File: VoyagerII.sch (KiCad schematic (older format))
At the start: 13 parts, among them U1 ATXMEGA32A4U-AU

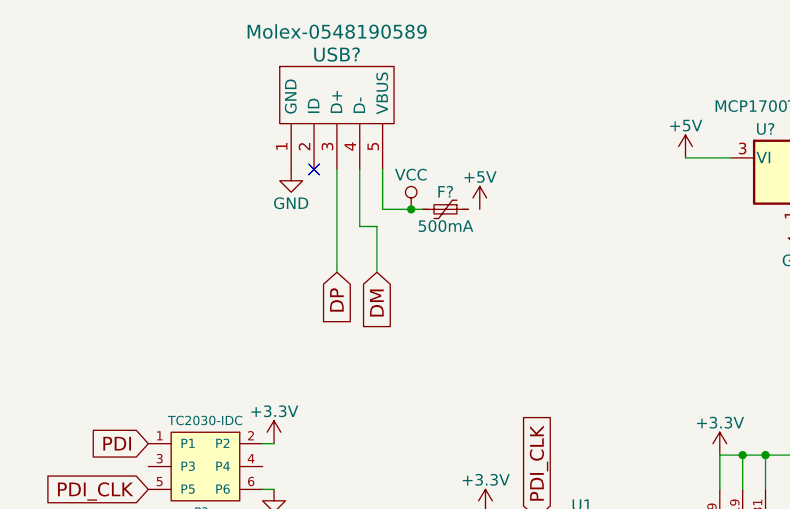
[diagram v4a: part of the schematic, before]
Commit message: Implement ESD protection
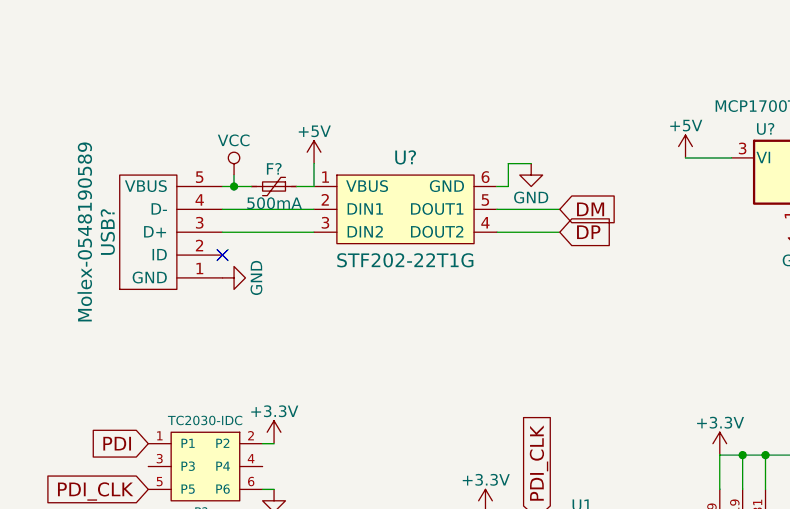
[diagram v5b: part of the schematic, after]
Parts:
- added U?: STF202-22T1G, symbol STF202-22T1G
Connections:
- net +5V: now also F?.1, U?.1 (VBUS)
- net DM: now also U?.5 (DOUT1); no longer USB?.4 (D-)
- net DP: now also U?.4 (DOUT2); no longer USB?.3 (D+)
- net GND: now also U?.6 (GND)
- new net: U?.3 (DIN2), USB?.3 (D+)
- new net: U?.2 (DIN1), USB?.4 (D-)
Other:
- moved on the sheet: F?, USB?
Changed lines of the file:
@@
 LIBS:ws2812b
 LIBS:Tag-Connect
+LIBS:ai03-locallib
 LIBS:VoyagerII-cache
 EELAYER 25 0
@@
 L Molex-0548190589 USB?
 U 1 1 5A624295
-P 1925 925
-F 0 "USB?" H 1925 1125 60  0000 C CNN
-F 1 "Molex-0548190589" H 1925 1225 60  0000 C CNN
-F 2 "" H 1925 925 60  0001 C CNN
-F 3 "" H 1925 925 60  0001 C CNN
-	1    1925 925
-	1    0    0    -1
-$EndComp
-Text GLabel 1925 1675 3    60   Input ~ 0
+P 1125 1500
+F 0 "USB?" H 1125 1700 60  0000 C CNN
+F 1 "Molex-0548190589" H 1125 1800 60  0000 C CNN
+F 2 "" H 1125 1500 60  0001 C CNN
+F 3 "" H 1125 1500 60  0001 C CNN
+	1    1125 1500
+	0    -1   -1   0
+$EndComp
+Text GLabel 2900 1500 2    60   Input ~ 0
 DP
-Text GLabel 2100 1675 3    60   Input ~ 0
+Text GLabel 2900 1400 2    60   Input ~ 0
 DM
 $Comp
 L Polyfuse_Small F?
 U 1 1 5A62446D
-P 2400 1400
-F 0 "F?" V 2325 1400 50  0000 C CNN
-F 1 "500mA" V 2475 1400 50  0000 C CNN
-F 2 "" H 2450 1200 50  0001 L CNN
-F 3 "" H 2400 1400 50  0001 C CNN
-	1    2400 1400
+P 1650 1300
+F 0 "F?" V 1575 1300 50  0000 C CNN
+F 1 "500mA" V 1725 1300 50  0000 C CNN
+F 2 "" H 1700 1100 50  0001 L CNN
+F 3 "" H 1650 1300 50  0001 C CNN
+	1    1650 1300
 	0    1    1    0
 $EndComp
@@
 L VCC #PWR?
 U 1 1 5A6244BE
-P 2250 1400
-F 0 "#PWR?" H 2250 1250 50  0001 C CNN
-F 1 "VCC" H 2250 1550 50  0000 C CNN
-F 2 "" H 2250 1400 50  0001 C CNN
-F 3 "" H 2250 1400 50  0001 C CNN
-	1    2250 1400
+P 1475 1250
+F 0 "#PWR?" H 1475 1100 50  0001 C CNN
+F 1 "VCC" H 1475 1400 50  0000 C CNN
+F 2 "" H 1475 1250 50  0001 C CNN
+F 3 "" H 1475 1250 50  0001 C CNN
+	1    1475 1250
 	1    0    0    -1
 $EndComp
@@
 L +5V #PWR?
 U 1 1 5A6244DC
-P 2550 1400
-F 0 "#PWR?" H 2550 1250 50  0001 C CNN
-F 1 "+5V" H 2550 1540 50  0000 C CNN
-F 2 "" H 2550 1400 50  0001 C CNN
-F 3 "" H 2550 1400 50  0001 C CNN
-	1    2550 1400
-	1    0    0    -1
-$EndComp
-NoConn ~ 1825 1225
+P 1825 1200
+F 0 "#PWR?" H 1825 1050 50  0001 C CNN
+F 1 "+5V" H 1825 1340 50  0000 C CNN
+F 2 "" H 1825 1200 50  0001 C CNN
+F 3 "" H 1825 1200 50  0001 C CNN
+	1    1825 1200
+	1    0    0    -1
+$EndComp
+NoConn ~ 1425 1600
 $Comp
 L GND #PWR?
 U 1 1 5A62457F
-P 1725 1225
-F 0 "#PWR?" H 1725 975 50  0001 C CNN
-F 1 "GND" H 1725 1075 50  0000 C CNN
-F 2 "" H 1725 1225 50  0001 C CNN
-F 3 "" H 1725 1225 50  0001 C CNN
-	1    1725 1225
-	1    0    0    -1
+P 1425 1700
+F 0 "#PWR?" H 1425 1450 50  0001 C CNN
+F 1 "GND" H 1425 1550 50  0000 C CNN
+F 2 "" H 1425 1700 50  0001 C CNN
+F 3 "" H 1425 1700 50  0001 C CNN
+	1    1425 1700
+	0    -1   -1   0
 $EndComp
 $Comp
@@
 $EndComp
 Wire Wire Line
-	1925 1225 1925 1675
-Wire Wire Line
-	2025 1225 2025 1475
-Wire Wire Line
-	2025 1475 2100 1475
-Wire Wire Line
-	2125 1225 2125 1400
-Wire Wire Line
-	2125 1400 2300 1400
-Wire Wire Line
 	4250 1175 4525 1175
 Connection ~ 4325 1175
@@
 Connection ~ 4625 2075
 Connection ~ 4825 2075
-Wire Wire Line
-	2100 1475 2100 1675
-Connection ~ 2250 1400
 Wire Wire Line
 	3450 1175 3650 1175
@@
 Text GLabel 4600 2925 2    60   Input ~ 0
 COL14
+$Comp
+L STF202-22T1G U?
+U 1 1 5A62CB9C
+P 2225 1400
+F 0 "U?" H 2225 1625 60  0000 C CNN
+F 1 "STF202-22T1G" H 2225 1175 60  0000 C CNN
+F 2 "" H 2150 1400 60  0001 C CNN
+F 3 "" H 2150 1400 60  0001 C CNN
+	1    2225 1400
+	1    0    0    -1
+$EndComp
+Wire Wire Line
+	1425 1500 1825 1500
+Wire Wire Line
+	1825 1400 1425 1400
+Wire Wire Line
+	1825 1300 1825 1200
+$Comp
+L GND #PWR?
+U 1 1 5A62D560
+P 2775 1200
+F 0 "#PWR?" H 2775 950 50  0001 C CNN
+F 1 "GND" H 2775 1050 50  0000 C CNN
+F 2 "" H 2775 1200 50  0001 C CNN
+F 3 "" H 2775 1200 50  0001 C CNN
+	1    2775 1200
+	1    0    0    -1
+$EndComp
+Wire Wire Line
+	2625 1300 2675 1300
+Wire Wire Line
+	2675 1300 2675 1200
+Wire Wire Line
+	2675 1200 2775 1200
+Wire Wire Line
+	2900 1400 2625 1400
+Wire Wire Line
+	2900 1500 2625 1500
+Wire Wire Line
+	1475 1250 1475 1300
+Wire Wire Line
+	1425 1300 1550 1300
+Connection ~ 1475 1300
+Wire Wire Line
+	1750 1300 1825 1300
 $EndSCHEMATC

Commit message: Bind controller footprints
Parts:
- C1, C2, C3, C4, C5, C6: renamed from C?; footprint (none) -> Capacitors_SMD:C_0805
- F1: renamed from F?; footprint (none) -> Fuse_Holders_and_Fuses:Fuse_SMD1206_Wave
- R1: renamed from R?; footprint (none) -> Resistors_SMD:R_0805
- SW1: renamed from SW?; footprint (none) -> Molex-0548190589:PushButton_6x6mm_TH
- U3: renamed from U?; footprint (none) -> Housings_SSOP:TSOP-6_1.65x3.05mm_Pitch0.95mm
- USB1: renamed from USB?; footprint (none) -> Molex-0548190589:Molex-0548190589
- gave numbers to parts that had none: 2
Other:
- moved on the sheet: C1, C2, C3, C4, C5, C6, R1, SW1, U1, U2
